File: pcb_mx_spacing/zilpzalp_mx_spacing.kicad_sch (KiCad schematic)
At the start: 43 parts, among them SW1 SW_Push, SW10 SW_Push, SW11 SW_Push, SW12 SW_Push, SW13 SW_Push, SW14 SW_Push, SW15 SW_Push, SW16 SW_Push, SW17 SW_Push, SW18 SW_Push, SW19 SW_Push, SW2 SW_Push, SW20 SW_Push, SW21 SW_Push, SW22 SW_Push, SW23 SW_Push, SW24 SW_Push, SW25 SW_Push, SW26 SW_Push, SW27 SW_Push, SW28 SW_Push, SW3 SW_Push, SW4 SW_Push, SW5 SW_Push, SW6 SW_Push, SW7 SW_Push, SW8 SW_Push, SW9 SW_Push, U1 xiao

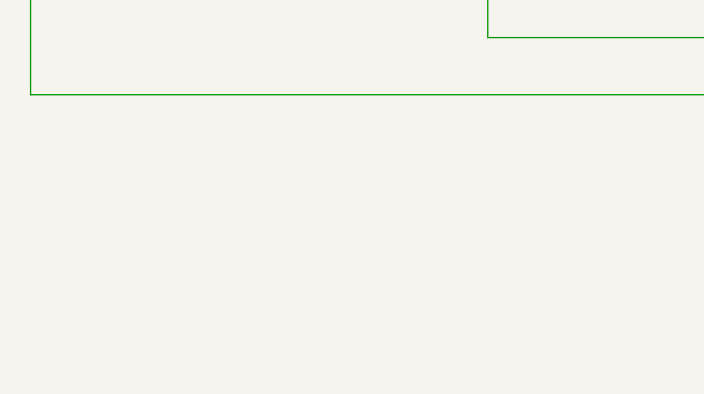
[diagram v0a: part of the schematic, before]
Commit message: add mounting holes
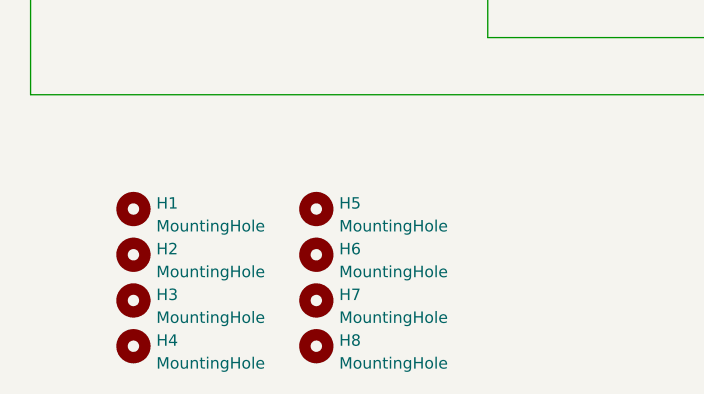
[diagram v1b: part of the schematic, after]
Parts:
- added H1, H2, H3, H4, H5, H6, H7, H8: MountingHole, BeiBob:MountingHole_3.5mm_no_silk, symbol Mechanical:MountingHole
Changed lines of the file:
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@@
+    )
+  )
+  (symbol (lib_id "Mechanical:MountingHole") (at 58.42 162.56 0) (unit 1)
+    (in_bom yes) (on_board yes) (dnp no) (fields_autoplaced)
+    (property "Reference" "H7" (at 60.96 161.925 0)
+      (effects (font (size 1.27 1.27)) (justify left))
+    )
+    (property "Value" "MountingHole" (at 60.96 164.465 0)
+      (effects (font (size 1.27 1.27)) (justify left))
+    )
+    (property "Footprint" "BeiBob:MountingHole_3.5mm_no_silk" (at 58.42 162.56 0)
+      (effects (font (size 1.27 1.27)) hide)
+    )
+    (property "Datasheet" "~" (at 58.42 162.56 0)
+      (effects (font (size 1.27 1.27)) hide)
+    )
+    (instances
+      (project "zilpzalp_mx_spacing"
+        (path "/5ecac6d8-0277-4350-80c1-88a8cf49a228"
+          (reference "H7") (unit 1)
+        )
+      )
     )
   )
@@
         (path "/5ecac6d8-0277-4350-80c1-88a8cf49a228"
           (reference "SW21") (unit 1)
+        )
+      )
+    )
+  )
+  (symbol (lib_id "Mechanical:MountingHole") (at 38.1 167.64 0) (unit 1)
+    (in_bom yes) (on_board yes) (dnp no) (fields_autoplaced)
+    (property "Reference" "H4" (at 40.64 167.005 0)
+      (effects (font (size 1.27 1.27)) (justify left))
+    )
+    (property "Value" "MountingHole" (at 40.64 169.545 0)
+      (effects (font (size 1.27 1.27)) (justify left))
+    )
+    (property "Footprint" "BeiBob:MountingHole_3.5mm_no_silk" (at 38.1 167.64 0)
+      (effects (font (size 1.27 1.27)) hide)
+    )
+    (property "Datasheet" "~" (at 38.1 167.64 0)
+      (effects (font (size 1.27 1.27)) hide)
+    )
+    (instances
+      (project "zilpzalp_mx_spacing"
+        (path "/5ecac6d8-0277-4350-80c1-88a8cf49a228"
+          (reference "H4") (unit 1)
         )
       )
@@
     )
   )
+  (symbol (lib_id "Mechanical:MountingHole") (at 58.42 167.64 0) (unit 1)
+    (in_bom yes) (on_board yes) (dnp no) (fields_autoplaced)
+    (property "Reference" "H8" (at 60.96 167.005 0)
+      (effects (font (size 1.27 1.27)) (justify left))
+    )
+    (property "Value" "MountingHole" (at 60.96 169.545 0)
+      (effects (font (size 1.27 1.27)) (justify left))
+    )
+    (property "Footprint" "BeiBob:MountingHole_3.5mm_no_silk" (at 58.42 167.64 0)
+      (effects (font (size 1.27 1.27)) hide)
+    )
+    (property "Datasheet" "~" (at 58.42 167.64 0)
+      (effects (font (size 1.27 1.27)) hide)
+    )
+    (instances
+      (project "zilpzalp_mx_spacing"
+        (path "/5ecac6d8-0277-4350-80c1-88a8cf49a228"
+          (reference "H8") (unit 1)
+        )
+      )
+    )
+  )
   (symbol (lib_id "MarBastLib-Various:BAV70_Small") (at 201.93 105.41 0) (mirror y) (unit 1)
     (in_bom yes) (on_board yes) (dnp no)
@@
     )
   )
+  (symbol (lib_id "Mechanical:MountingHole") (at 58.42 152.4 0) (unit 1)
+    (in_bom yes) (on_board yes) (dnp no) (fields_autoplaced)
+    (property "Reference" "H5" (at 60.96 151.765 0)
+      (effects (font (size 1.27 1.27)) (justify left))
+    )
+    (property "Value" "MountingHole" (at 60.96 154.305 0)
+      (effects (font (size 1.27 1.27)) (justify left))
+    )
+    (property "Footprint" "BeiBob:MountingHole_3.5mm_no_silk" (at 58.42 152.4 0)
+      (effects (font (size 1.27 1.27)) hide)
+    )
+    (property "Datasheet" "~" (at 58.42 152.4 0)
+      (effects (font (size 1.27 1.27)) hide)
+    )
+    (instances
+      (project "zilpzalp_mx_spacing"
+        (path "/5ecac6d8-0277-4350-80c1-88a8cf49a228"
+          (reference "H5") (unit 1)
+        )
+      )
+    )
+  )
   (symbol (lib_id "Switch:SW_Push") (at 57.15 50.8 0) (unit 1)
     (in_bom yes) (on_board yes) (dnp no) (fields_autoplaced)
@@
     )
   )
+  (symbol (lib_id "Mechanical:MountingHole") (at 38.1 152.4 0) (unit 1)
+    (in_bom yes) (on_board yes) (dnp no) (fields_autoplaced)
+    (property "Reference" "H1" (at 40.64 151.765 0)
+      (effects (font (size 1.27 1.27)) (justify left))
+    )
+    (property "Value" "MountingHole" (at 40.64 154.305 0)
+      (effects (font (size 1.27 1.27)) (justify left))
+    )
+    (property "Footprint" "BeiBob:MountingHole_3.5mm_no_silk" (at 38.1 152.4 0)
+      (effects (font (size 1.27 1.27)) hide)
+    )
+    (property "Datasheet" "~" (at 38.1 152.4 0)
+      (effects (font (size 1.27 1.27)) hide)
+    )
+    (instances
+      (project "zilpzalp_mx_spacing"
+        (path "/5ecac6d8-0277-4350-80c1-88a8cf49a228"
+          (reference "H1") (unit 1)
+        )
+      )
+    )
+  )
   (symbol (lib_id "Switch:SW_Push") (at 189.23 101.6 0) (unit 1)
     (in_bom yes) (on_board yes) (dnp no) (fields_autoplaced)
@@
     )
   )
+  (symbol (lib_id "Mechanical:MountingHole") (at 38.1 157.48 90) (unit 1)
+    (in_bom yes) (on_board yes) (dnp no) (fields_autoplaced)
+    (property "Reference" "H2" (at 40.64 156.845 90)
+      (effects (font (size 1.27 1.27)) (justify right))
+    )
+    (property "Value" "MountingHole" (at 40.64 159.385 90)
+      (effects (font (size 1.27 1.27)) (justify right))
+    )
+    (property "Footprint" "BeiBob:MountingHole_3.5mm_no_silk" (at 38.1 157.48 0)
+      (effects (font (size 1.27 1.27)) hide)
+    )
+    (property "Datasheet" "~" (at 38.1 157.48 0)
+      (effects (font (size 1.27 1.27)) hide)
+    )
+    (instances
+      (project "zilpzalp_mx_spacing"
+        (path "/5ecac6d8-0277-4350-80c1-88a8cf49a228"
+          (reference "H2") (unit 1)
+        )
+      )
+    )
+  )
   (symbol (lib_id "MarBastLib-Various:BAV70_Small") (at 95.25 29.21 0) (mirror y) (unit 1)
     (in_bom yes) (on_board yes) (dnp no)
@@
     )
   )
+  (symbol (lib_id "Mechanical:MountingHole") (at 38.1 162.56 0) (unit 1)
+    (in_bom yes) (on_board yes) (dnp no) (fields_autoplaced)
+    (property "Reference" "H3" (at 40.64 161.925 0)
+      (effects (font (size 1.27 1.27)) (justify left))
+    )
+    (property "Value" "MountingHole" (at 40.64 164.465 0)
+      (effects (font (size 1.27 1.27)) (justify left))
+    )
+    (property "Footprint" "BeiBob:MountingHole_3.5mm_no_silk" (at 38.1 162.56 0)
+      (effects (font (size 1.27 1.27)) hide)
+    )
+    (property "Datasheet" "~" (at 38.1 162.56 0)
+      (effects (font (size 1.27 1.27)) hide)
+    )
+    (instances
+      (project "zilpzalp_mx_spacing"
+        (path "/5ecac6d8-0277-4350-80c1-88a8cf49a228"
+          (reference "H3") (unit 1)
+        )
+      )
+    )
+  )
   (symbol (lib_id "MarBastLib-Various:BAV70_Small") (at 44.45 80.01 0) (mirror y) (unit 1)
     (in_bom yes) (on_board yes) (dnp no)
@@
         )
       )
+    )
+  )
+  (symbol (lib_id "Mechanical:MountingHole") (at 58.42 157.48 0) (unit 1)
+    (in_bom yes) (on_board yes) (dnp no) (fields_autoplaced)
+    (property "Reference" "H6" (at 60.96 156.845 0)
+      (effects (font (size 1.27 1.27)) (justify left))
+    )
+    (property "Value" "MountingHole" (at 60.96 159.385 0)
+      (effects (font (size 1.27 1.27)) (justify left))
+    )
+    (property "Footprint" "BeiBob:MountingHole_3.5mm_no_silk" (at 58.42 157.48 0)
+      (effects (font (size 1.27 1.27)) hide)
+    )
+    (property "Datasheet" "~" (at 58.42 157.48 0)
+      (effects (font (size 1.27 1.27)) hide)
+    )
+    (instances
+      (project "zilpzalp_mx_spacing"
+        (path "/5ecac6d8-0277-4350-80c1-88a8cf49a228"
+          (reference "H6") (unit 1)
+        )
+      )
